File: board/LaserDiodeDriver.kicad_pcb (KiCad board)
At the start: 2 copper layers, 45.7 x 45.7 mm, 51 parts, among them J1 Conn_01x02, Q1 2N7002, Q2 IRF9Z34, SW2 SW_DPDT_x2, U1 LT1009, U2 OPA4192, U3 LM317

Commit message: Final touches :)
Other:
- board text added: "(Bottom View)"
- board text added: "1"
- board text added: "2"
- board text added: "3"
- board text added: "CC CP"
- board text added: "I_{LD}"
- board text added: "I_{PD}"
- board text added: "Thorlabs: C Type Laser Diode Driver Rev:#1 Drew Wellen"
- board text removed: "Laser Diode Driver Rev: 1 Drew Wellen"

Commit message: Final Final touches. Added indicator LEDs.
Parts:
- added D4: LED (Blue), LED_SMD:LED_0603_1608Metric, F.Cu at (159.7, 95.4)
- added D5: LED (Yellow), LED_SMD:LED_0603_1608Metric, F.Cu at (158.0, 95.4)
- added G***: LOGO, LOGO, B.Cu at (127.0, 93.3)
- added R18: 345, Resistor_SMD:R_0603_1608Metric, F.Cu at (159.7, 92.3)
- added R2: 500, Resistor_SMD:R_0603_1608Metric, F.Cu at (158.0, 92.3)
- added REF**: WEEE-Logo_4.2x6mm_SilkScreen, Symbol:WEEE-Logo_4.2x6mm_SilkScreen, B.Cu at (129.2, 125.2)
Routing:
- net +12V: track 50.3 -> 65.9 mm
- net GND: track 38.4 -> 42.1 mm, vias 8 -> 9
- net Net-(D5-A): track 0.00 -> 1.50 mm
- net Net-(D4-A): track 0.00 -> 1.49 mm

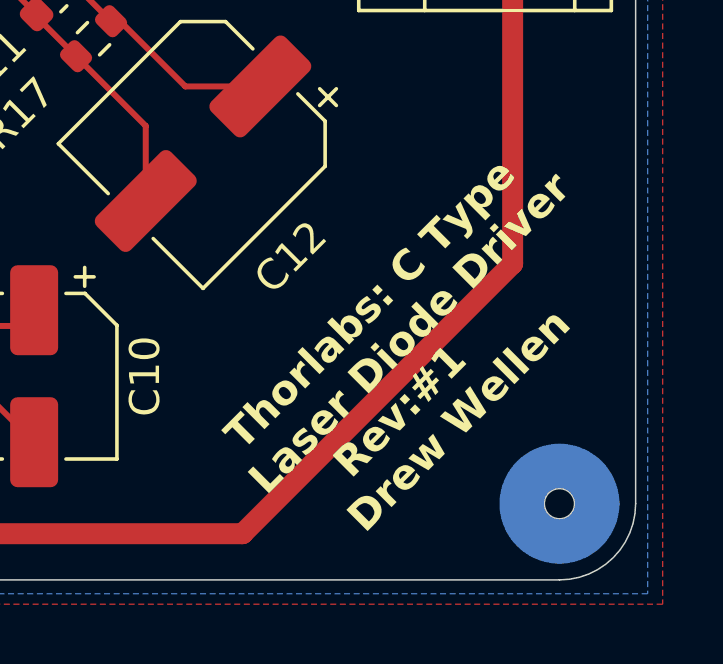
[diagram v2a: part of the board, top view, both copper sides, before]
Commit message: Added date to silkscreen
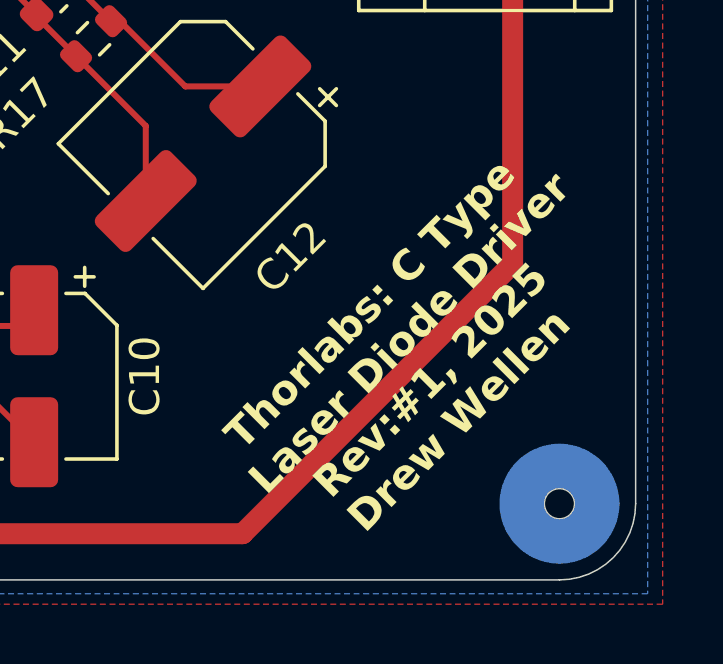
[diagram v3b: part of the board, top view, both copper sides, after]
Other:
- board text added: "Thorlabs: C Type Laser Diode Driver Rev:#1, 2025 Drew Wellen"
- board text removed: "Thorlabs: C Type Laser Diode Driver Rev:#1 Drew Wellen"
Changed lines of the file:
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@@
 		(layer "Edge.Cuts")
 	)
-	(gr_text " Thorlabs: C Type\nLaser Diode Driver\n	 Rev:#1\n   Drew Wellen"
+	(gr_text " Thorlabs: C Type\nLaser Diode Driver\n   Rev:#1, 2025\n   Drew Wellen"
 		(at 155.15 129.1 45)
 		(layer "F.SilkS")

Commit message: Layout review initial changes
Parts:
- removed REF**: WEEE-Logo_4.2x6mm_SilkScreen, Symbol:WEEE-Logo_4.2x6mm_SilkScreen
- R14: footprint Resistor_SMD:R_0603_1608Metric -> Resistor_SMD:R_0603_1608Metric_Pad0.98x0.95mm_HandSolder
- R16: footprint Capacitor_SMD:C_0603_1608Metric_Pad1.08x0.95mm_HandSolder -> Resistor_SMD:R_0603_1608Metric_Pad0.98x0.95mm_HandSolder
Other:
- board text added: "Thorlabs: C Type Laser Diode Driver Rev:#1, 2026 Drew Wellen"
- board text removed: "Thorlabs: C Type Laser Diode Driver Rev:#1, 2025 Drew Wellen"

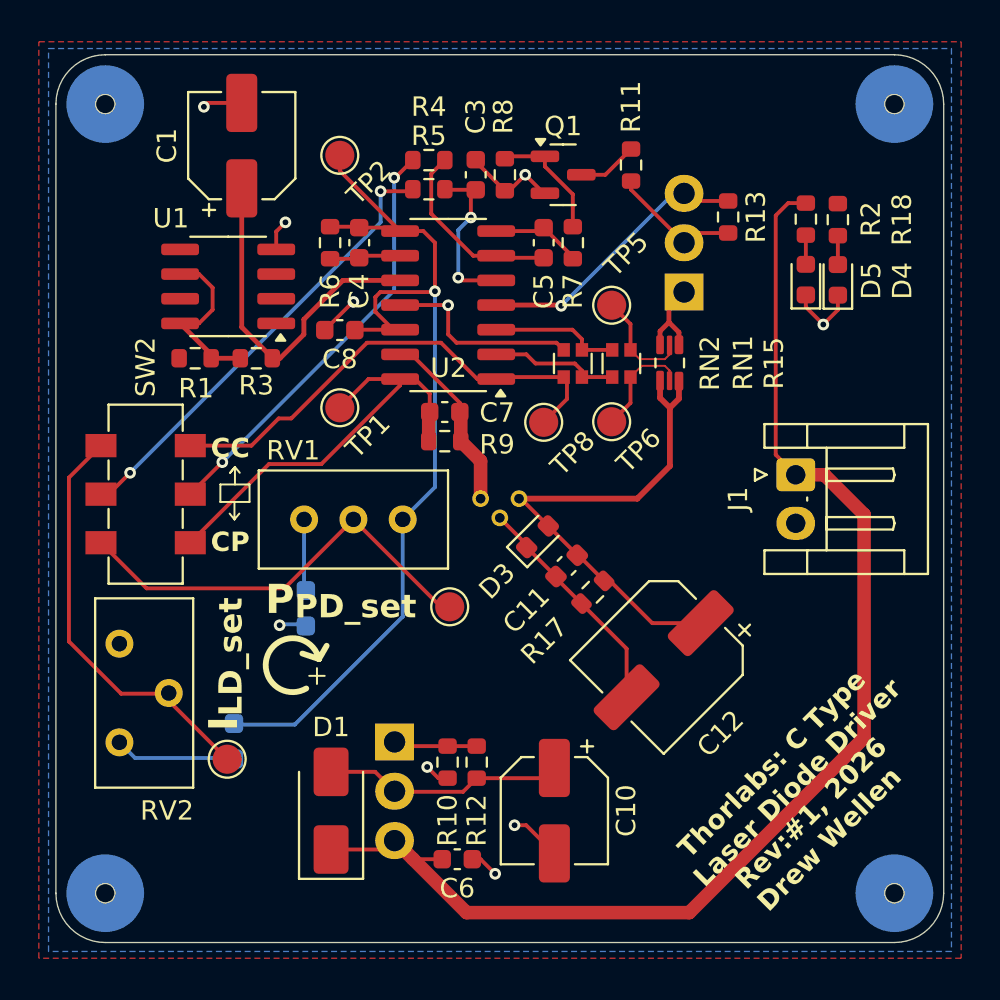
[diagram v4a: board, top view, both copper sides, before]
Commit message: Post layout review fixes. Ready for CDR and ordering
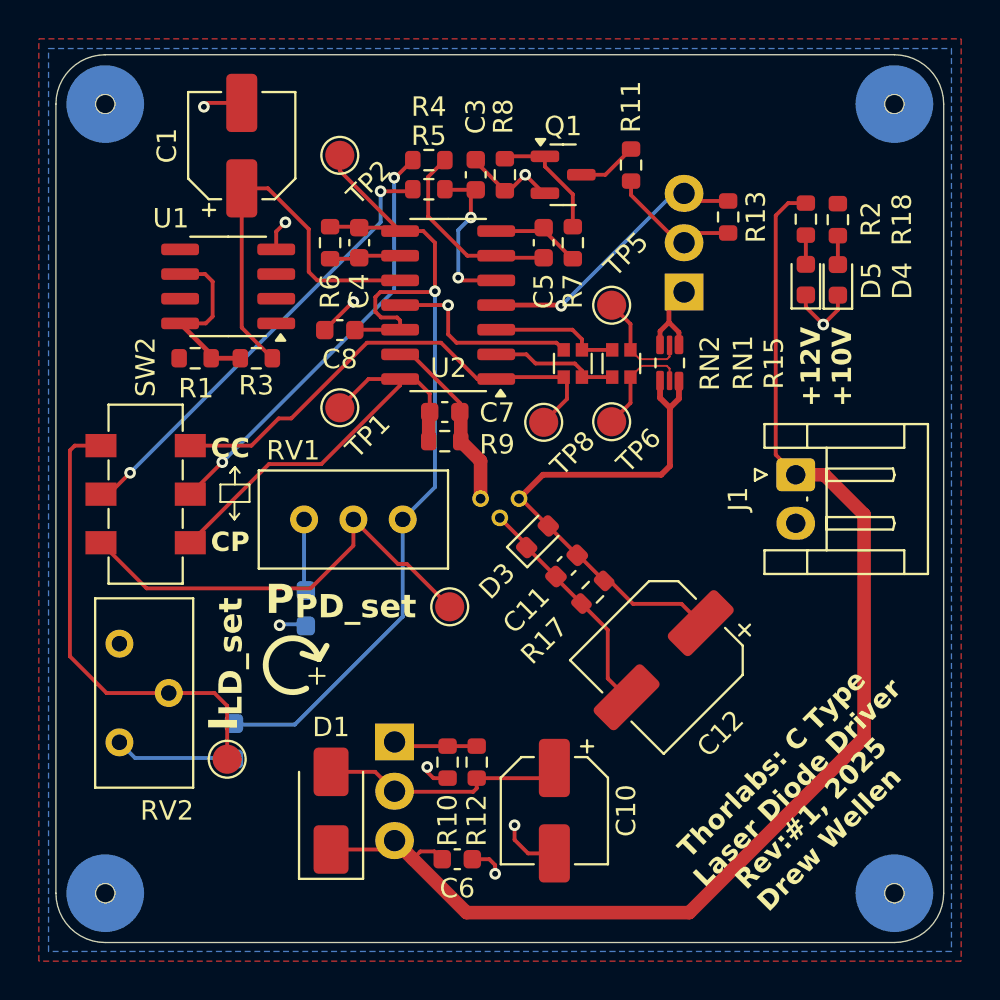
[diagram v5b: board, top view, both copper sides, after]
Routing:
- net I_{LD_set}: track 21.4 -> 24.2 mm
- net Net-(U2C-+): track 18.1 -> 20.8 mm
- net GND: track 42.1 -> 42.9 mm
- net P_{PD_set}: track 22.3 -> 23.1 mm
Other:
- board text added: "+12V +10V"
- board text added: "Thorlabs: C Type Laser Diode Driver Rev:#1, 2025 Drew Wellen"
- board text removed: "Thorlabs: C Type Laser Diode Driver Rev:#1, 2026 Drew Wellen"
